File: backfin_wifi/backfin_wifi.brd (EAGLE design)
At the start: 68.6 x 53.3 mm, 31 parts, among them SW1 SPST_TACT-EVQQ2, U1 CC3000MOD, U7 TLV70236SOT23-5, U8 TXB0106TSSOP16

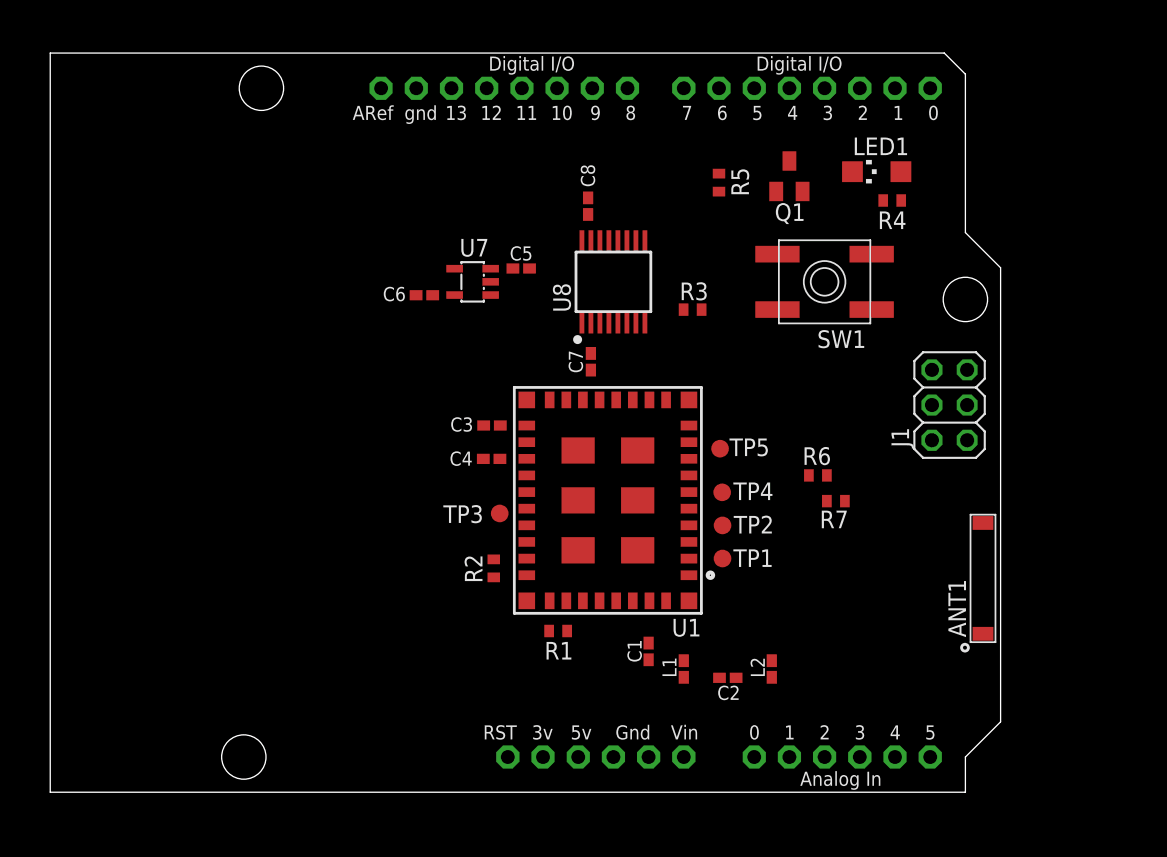
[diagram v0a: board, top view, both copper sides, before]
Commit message: Only transmission line remains...
Contacted 4PCB to see what their $33 standard stackup is.
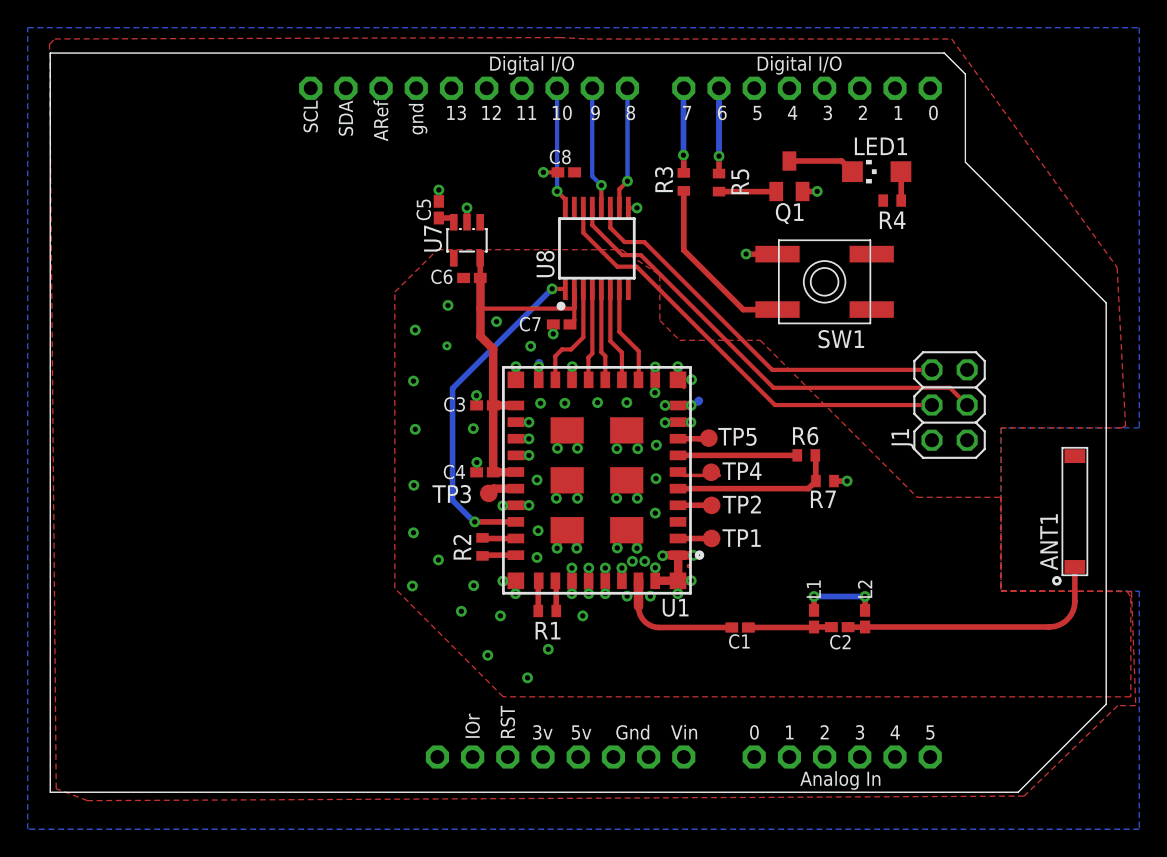
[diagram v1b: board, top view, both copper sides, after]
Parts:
- removed U$2: ARDUINOUNO, adafruit:ARDUINO
- added U2: ARDUINOR3-DIMENSION, custom:ARDUINOR3
- moved L1 10.1 mm to (55.1, 12.5)
- moved R3 9.24 mm to (45.7, 44.0), turned to 270 degrees
- moved C2 8.87 mm to (57.0, 11.9)
- moved ANT1 8.20 mm to (73.9, 16.3)
- moved L2 7.65 mm to (58.8, 12.5)
- moved C5 7.30 mm to (28.0, 42.0), turned to 90 degrees
- moved C1 6.83 mm to (49.8, 11.9), turned to 180 degrees
- moved C6 3.65 mm to (30.4, 37.1)
- moved C7 3.42 mm to (36.9, 33.8), turned to 0 degrees
- moved U7 3.02 mm to (30.1, 39.8), turned to 180 degrees
- moved C8 2.90 mm to (37.2, 44.7), turned to 0 degrees
- moved U8 2.69 mm to (39.4, 39.2)
- moved R2 1.75 mm to (31.2, 17.7)
- moved R6 1.67 mm to (54.6, 24.3)
- moved TP1 1.65 mm to (47.7, 18.3)
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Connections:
- net +3V3: now also U2.3V; no longer U$2.3V
- net +5V: now also U2.5V; no longer U$2.5V
- net GND: now also U2.GND, U2.GND1, U2.GND2; no longer U$2.GND, U$2.GND1, U$2.GND2
- net N$17: now also U2.D7; no longer U$2.D7
- net N$19: now also U2.D6; no longer U$2.D6
- net SPI_CS_HOST: now also U2.D10; no longer U$2.D10
- net SPI_IRQ_HOST: now also U2.D9; no longer U$2.D9
- net VBAT_SW_EN: now also U2.D8; no longer U$2.D8
- net VIN: now also U2.VIN; no longer U$2.VIN
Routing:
- net GND: track 0.00 -> 45.4 mm, vias 0 -> 87
- net SPI_DIN_HOST: track 0.00 -> 33.7 mm
- net SPI_CLK_HOST: track 0.00 -> 32.1 mm
- net VCC: track 0.00 -> 30.0 mm
- net SPI_DOUT_HOST: track 0.00 -> 28.9 mm
- net N$16: track 0.00 -> 24.4 mm, vias 0 -> 2
- net N$15: track 0.00 -> 19.7 mm
- net N$18: track 0.00 -> 12.8 mm
- net N$2: track 0.00 -> 12.1 mm
- net N$12: track 0.00 -> 9.34 mm
- net SPI_IRQ_HOST: track 0.00 -> 8.90 mm, vias 0 -> 1
- net SPI_CS_HOST: track 0.00 -> 8.88 mm, vias 0 -> 1
- net VBAT_SW_EN: track 0.00 -> 8.87 mm, vias 0 -> 1
- net N$1: track 0.00 -> 8.61 mm
- net WL_SPI_CLK_HOST: track 0.00 -> 7.79 mm
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- added copper zone on layer 1, net +5V
- added copper zone on layer 1, net GND
- added copper zone on layer 16, net GND
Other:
- board size 68.6 x 53.3 mm -> 76.2 x 53.3 mm

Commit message: Waveguide complete....
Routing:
- net N$23: track 1.75 -> 0.00 mm
- net GND: vias 87 -> 159

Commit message: Ready for ordering...
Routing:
- net VCC: track 30.0 -> 36.3 mm
- net GND: track 45.4 -> 41.8 mm, vias 159 -> 161
